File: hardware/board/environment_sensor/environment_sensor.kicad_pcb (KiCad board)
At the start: 4 copper layers, 39.9 x 28 mm, 56 parts, among them J2 AudioJack3, J3 USB_C_Receptacle_USB2.0, SW1 SW_Push, U1 TPD2EUSB30, U3 RP2040, U4 W25Q16JVUXIQ, U5 BME688, U6 rt6150b-33gqw, X1 ECS-TXO-2016

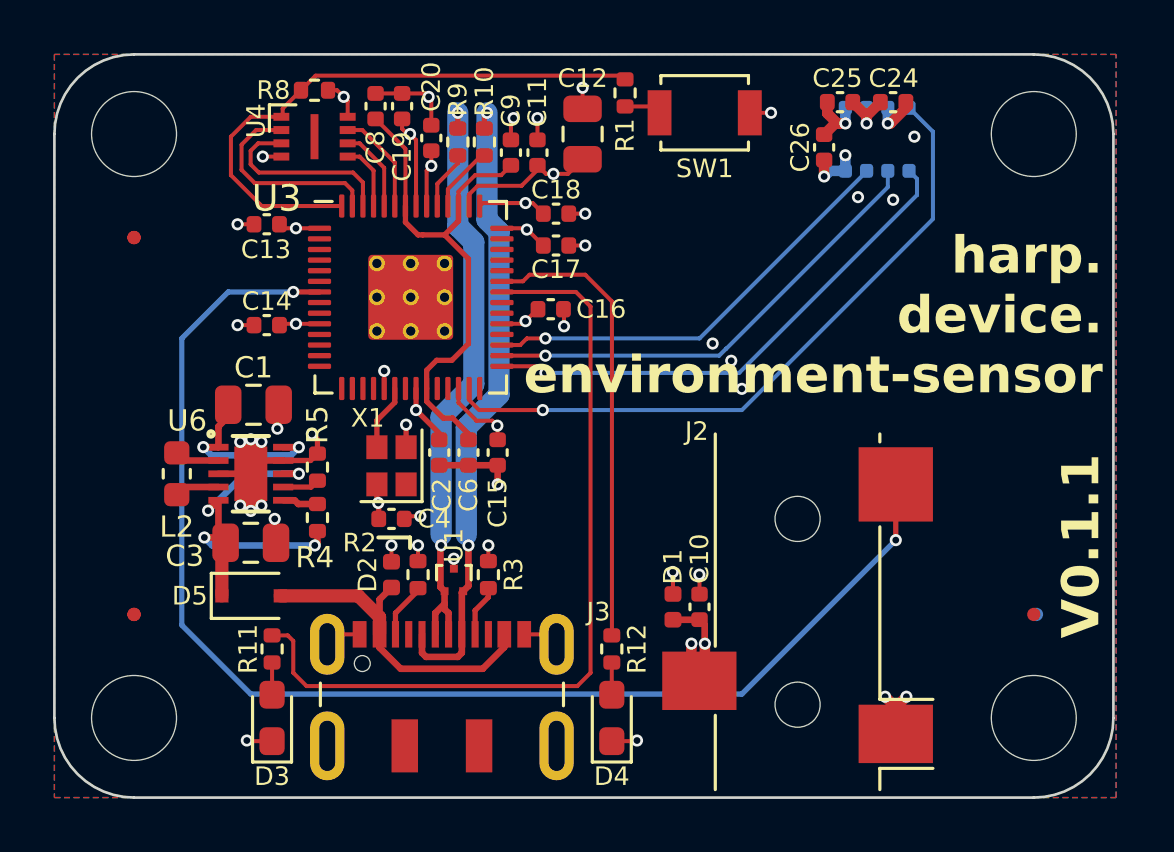
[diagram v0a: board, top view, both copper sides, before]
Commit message: update pcb thermal landing
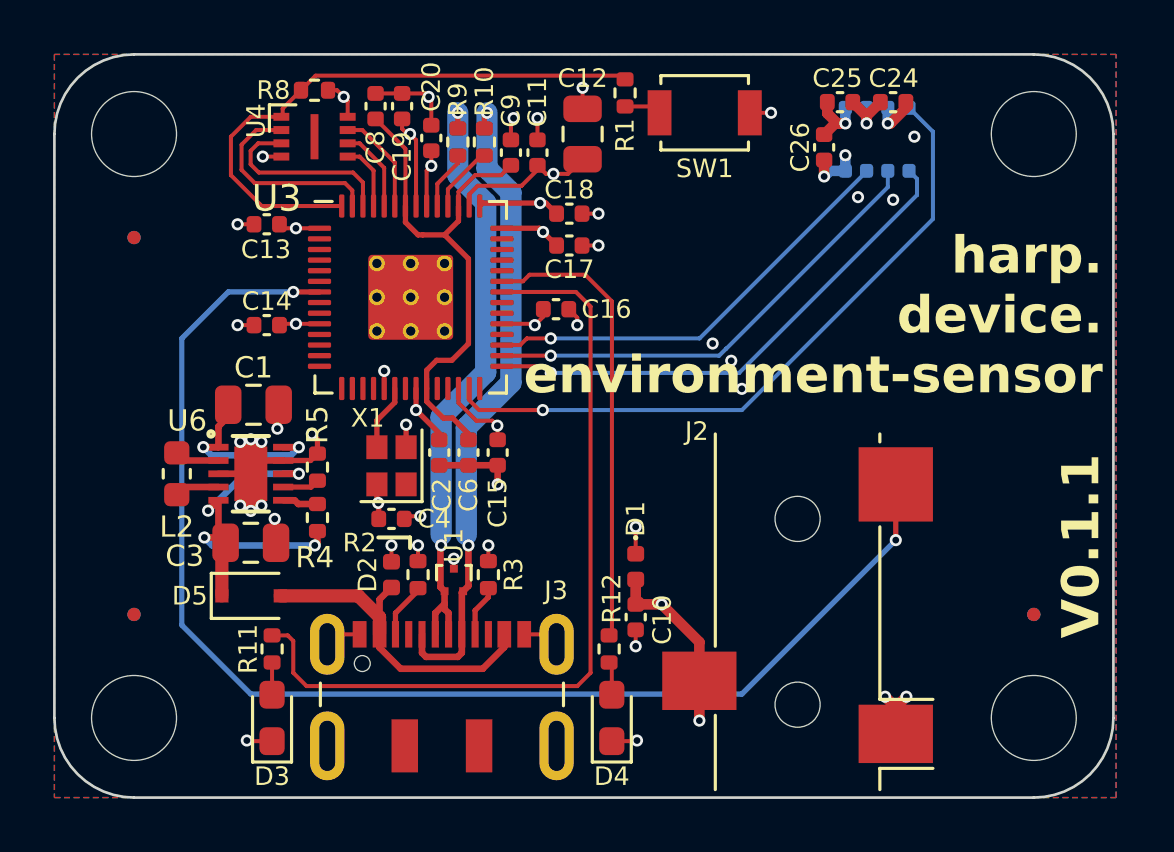
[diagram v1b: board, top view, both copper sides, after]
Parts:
- FID4, FID5: moved to B.Cu
- moved C10 2.44 mm to (145.9, 103.2), turned to -90 degrees
- moved D1 2.07 mm to (145.9, 101.3)
- moved C17 0.50 mm to (143.4, 89.2)
- moved C18 0.50 mm to (143.4, 88.0)
- moved C16 0.20 mm to (142.9, 91.6)
- moved FID6 0.10 mm to (160.9, 103.1)
- moved R12 0.10 mm to (144.9, 104.4)
- turned FID4 to 180 degrees
- turned FID5 to 180 degrees
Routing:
- net +3V3: track 44.8 -> 48.0 mm
